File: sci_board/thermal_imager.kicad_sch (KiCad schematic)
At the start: 1 part, among them J6 Conn_01x04_Pin

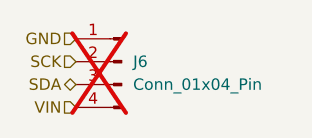
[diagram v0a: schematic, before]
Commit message: tweaking SCI and AUX for production, using common sheets as much as possible
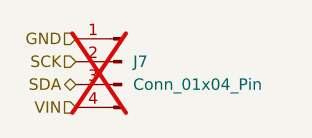
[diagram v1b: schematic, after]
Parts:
- renumbered J6 to J7
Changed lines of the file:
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@@
 		(dnp yes)
 		(fields_autoplaced yes)
-		(property "Reference" "J6"
+		(property "Reference" "J7"
 			(at 54.61 31.7499 0)
 			(effects
@@
 			(project ""
 				(path "/b4b2c88d-f6cd-4e60-862d-e21f68728580/b65d9c5b-bcd6-4ca1-83d4-ac547dcb4ba6"
-					(reference "J6")
+					(reference "J7")
 					(unit 1)
 				)

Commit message: clenup BOM for SCI and AUX
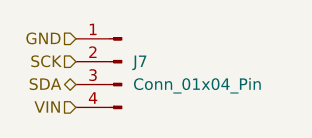
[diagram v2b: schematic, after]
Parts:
- J7: Manufacturer (none) -> generic; Part Number (none) -> generic; now fitted
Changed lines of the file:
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@@
 		(in_bom yes)
 		(on_board yes)
-		(dnp yes)
+		(dnp no)
 		(fields_autoplaced yes)
 		(property "Reference" "J7"
@@
 			(at 53.34 31.75 0)
 			(effects
+				(font
+					(size 1.27 1.27)
+				)
+				(hide yes)
+			)
+		)
+		(property "Manufacturer" "generic"
+			(at 53.34 31.75 0)
+			(effects
+				(font
+					(size 1.27 1.27)
+				)
+				(hide yes)
+			)
+		)
+		(property "Part Number" "generic"
+			(at 53.34 31.75 0)
+			(effects
